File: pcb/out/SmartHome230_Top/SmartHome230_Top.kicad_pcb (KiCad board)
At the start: 2 copper layers, 114 x 56 mm, 12 parts, among them J1 B2B, U1 MCP23017, U2 DS18B20

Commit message: Przekazniki do wnetrza (nie przy krawedzi); zaciski 230V zostaja na krawedzi
Rozdzielenie strefy 230V: zaciski sieciowe (dostep kablem) zlicowane przy dolnej
krawedzi, a przekazniki przeniesione do wnetrza w pas tuz nad zaciskami - z dala
od brzegu plytki (kolizja z obudowa). Logika pakowana nad strefa przekaznikow.
Powiekszona wspolna ramka (130x115) jako stala FRAME. SmartHome230 0/0/0, 11/11.

Co-Authored-By: Claude Opus 4.8 (1M context) <noreply@anthropic.com>
Claude-Session: https://claude.ai/code/session_01LNGxtK2Jv1rJLBLPTwFQ9C
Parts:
- moved H3 25.1 mm to (122.5, 92.5)
- moved H4 23.0 mm to (7.50, 92.5)
- moved J1 12.5 mm to (65.0, 57.5)
- moved H2 10.0 mm to (122.5, 22.5)
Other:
- board size 114 x 56 mm -> 124 x 79 mm
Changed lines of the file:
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@@
     "pcbforge:MountingHole_M3"
     (layer "F.Cu")
-    (at 112.5 22.5)
+    (at 122.5 22.5)
     (descr "Otwor montazowy M3")
     (attr through_hole)
@@
     "pcbforge:MountingHole_M3"
     (layer "F.Cu")
-    (at 112.5 69.5)
+    (at 122.5 92.5)
     (descr "Otwor montazowy M3")
     (attr through_hole)
@@
     "pcbforge:MountingHole_M3"
     (layer "F.Cu")
-    (at 7.5 69.5)
+    (at 7.5 92.5)
     (descr "Otwor montazowy M3")
     (attr through_hole)
@@
     "pcbforge:PinHeader_2x10_P2.54mm"
     (layer "F.Cu")
-    (at 60 46)
+    (at 65 57.5)
     (descr "Pin header 2x10")
     (attr through_hole)
@@
   (gr_line
     (start 3 18)
-    (end 117 18)
+    (end 127 18)
     (stroke
       (width 0.1)
@@
   )
   (gr_line
-    (start 117 18)
-    (end 117 74)
+    (start 127 18)
+    (end 127 97)
     (stroke
       (width 0.1)
@@
   )
   (gr_line
-    (start 117 74)
-    (end 3 74)
+    (start 127 97)
+    (end 3 97)
     (stroke
       (width 0.1)
@@
   )
   (gr_line
-    (start 3 74)
+    (start 3 97)
     (end 3 18)
     (stroke
@@
   (gr_text
     "SmartHome230_Top"
-    (at 2 90.5 0)
+    (at 2 113.5 0)
     (layer "F.SilkS")
     (effects
@@
   (gr_text
     "Plyta gorna (wezsza): ekspander I/O + ochrona"
-    (at 2 88 0)
+    (at 2 111 0)
     (layer "F.SilkS")
     (effects
@@
   (gr_text
     "Skladana na plyte glowna - otwory i zlacze pasuja 1:1"
-    (at 2 85.8 0)
+    (at 2 108.8 0)
     (layer "F.SilkS")
     (effects

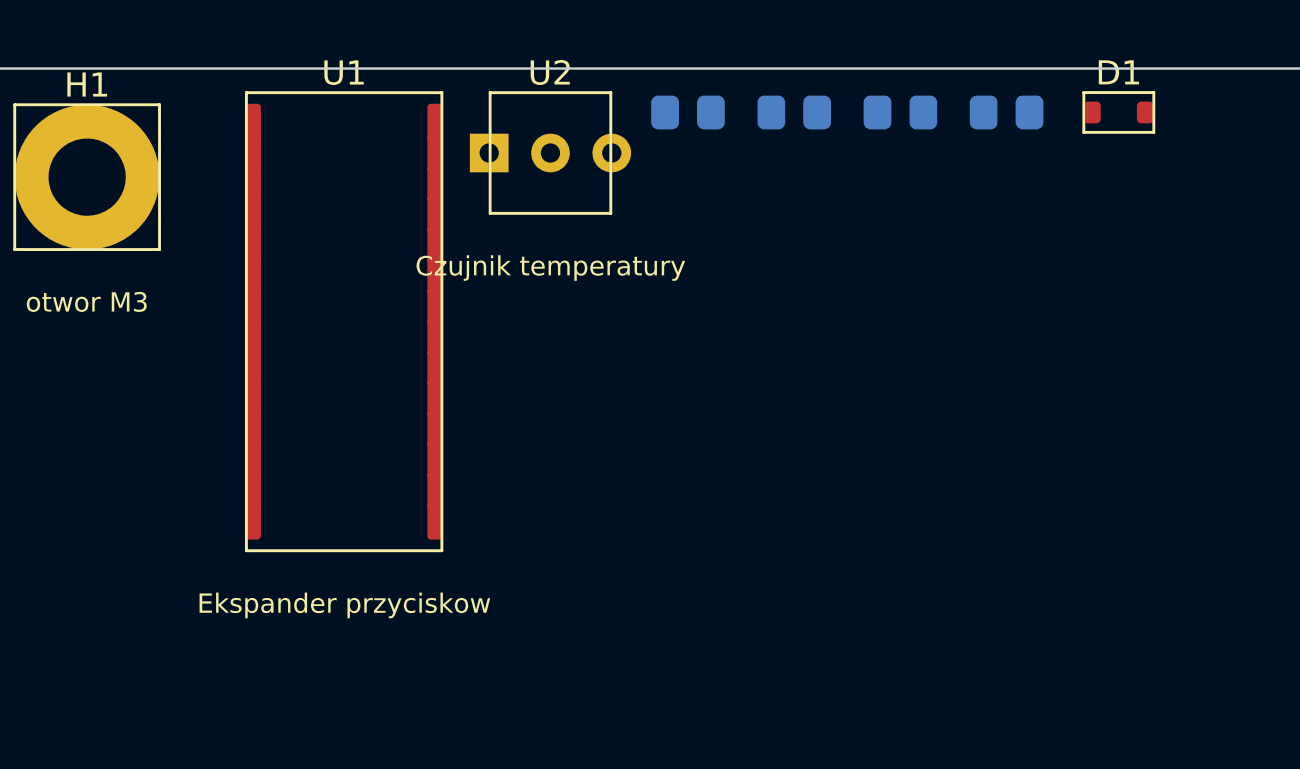
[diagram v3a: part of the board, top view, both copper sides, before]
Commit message: ESP32-S3 + przyciski TFT; kompaktowy layout (szerokosc z liczby zlacz, 2 rzedy)
- Przejscie ESP32-C3 -> ESP32-S3 (duzo GPIO): niezalezne RS485/CAN, dotyk z IRQ,
  4 przyciski nawigacji TFT (GORA/DOL/OK/WSTECZ). Nowa czesc ESP32-S3-WROOM-1.
- Layout: I/O wzdluz krawedzi w 2 rzedach (podwojne w pionie), szerokosc plytki
  wynika z LICZBY zlacz (zmienne szerokosci kolumn) - wejscia na gornej krawedzi,
  wyjscia (zaciski) na dolnej. auto_frame() dobiera ciasna wspolna ramke.
- Przekazniki pakowane w strefe 230V (kilka rzedow) omijajaca otwory.
- HomeCtrlPro: 280x185 -> 168x192 mm, mniej pustego miejsca. Oba 0/0/0.

Testy 12/12, zwalidowane kiutils. Bloki: esp32s3, button.

Co-Authored-By: Claude Opus 4.8 (1M context) <noreply@anthropic.com>
Claude-Session: https://claude.ai/code/session_01LNGxtK2Jv1rJLBLPTwFQ9C
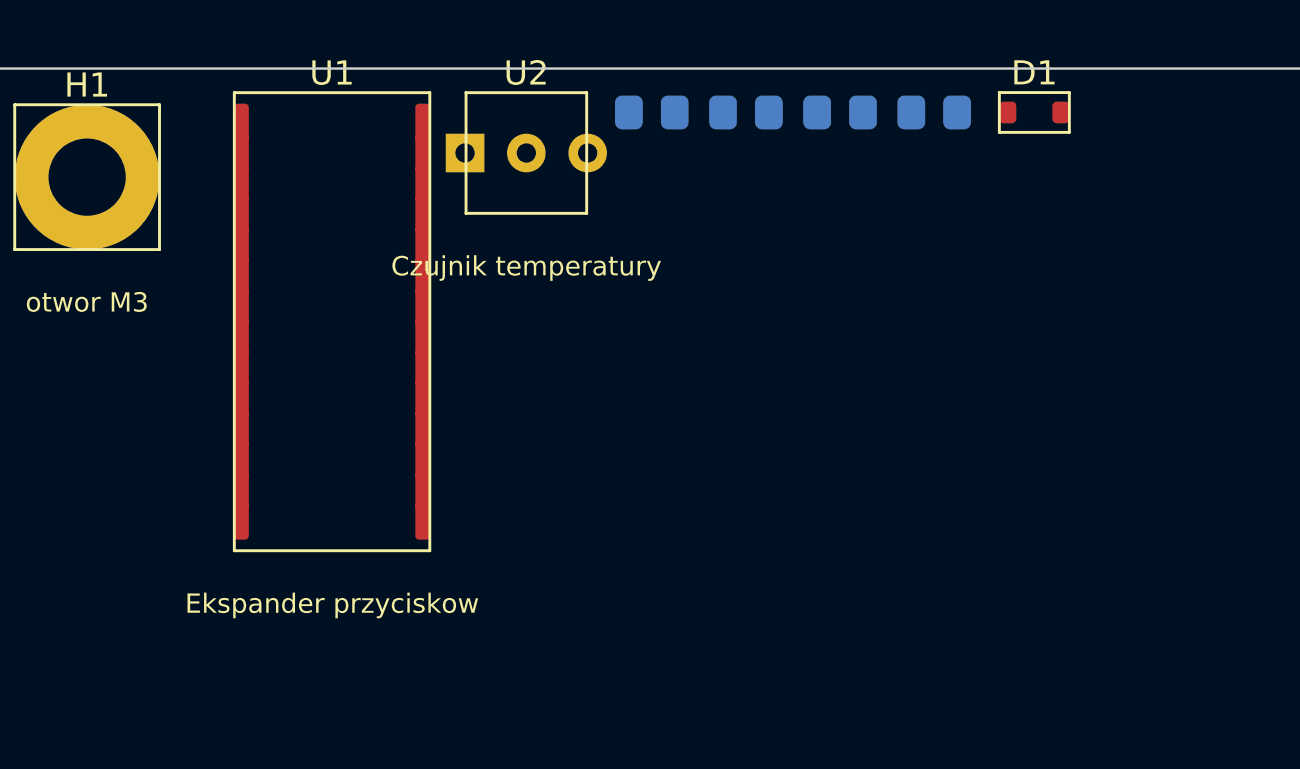
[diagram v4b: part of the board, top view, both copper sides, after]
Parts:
- moved D1 3.50 mm to (46.8, 19.8)
- moved R3 3.00 mm to (42.6, 19.8)
- moved R2 2.50 mm to (38.7, 19.8)
- moved R1 2.00 mm to (34.8, 19.8)
- moved C1 1.50 mm to (30.9, 19.8)
- moved U2 1.00 mm to (25.7, 21.5)
- moved U1 0.50 mm to (17.6, 28.5)
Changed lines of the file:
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@@
     "pcbforge:SOIC-28"
     (layer "F.Cu")
-    (at 18.15 28.49)
+    (at 17.65 28.49)
     (descr "SOIC-28 (1.27mm)")
     (attr smd)
@@
     "pcbforge:C_0805"
     (layer "B.Cu")
-    (at 32.4 19.82)
+    (at 30.9 19.82)
     (descr "C chip 0805")
     (attr smd)
@@
     "pcbforge:R_0805"
     (layer "B.Cu")
-    (at 36.8 19.82)
+    (at 34.8 19.82)
     (descr "R chip 0805")
     (attr smd)
@@
     "pcbforge:R_0805"
     (layer "B.Cu")
-    (at 41.2 19.82)
+    (at 38.7 19.82)
     (descr "R chip 0805")
     (attr smd)
@@
     "pcbforge:R_0805"
     (layer "B.Cu")
-    (at 45.6 19.82)
+    (at 42.6 19.82)
     (descr "R chip 0805")
     (attr smd)
@@
     "pcbforge:D_SOD-323"
     (layer "F.Cu")
-    (at 50.25 19.82)
+    (at 46.75 19.82)
     (descr "D_SOD-323")
     (attr smd)
@@
     "pcbforge:TO-92"
     (layer "F.Cu")
-    (at 26.7 21.5)
+    (at 25.7 21.5)
     (descr "TO-92")
     (attr through_hole)
